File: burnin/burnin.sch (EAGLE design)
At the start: 12 parts, among them M1 ARDUINO_R3_ICSP_NODIM, U1 TXB0104PWR

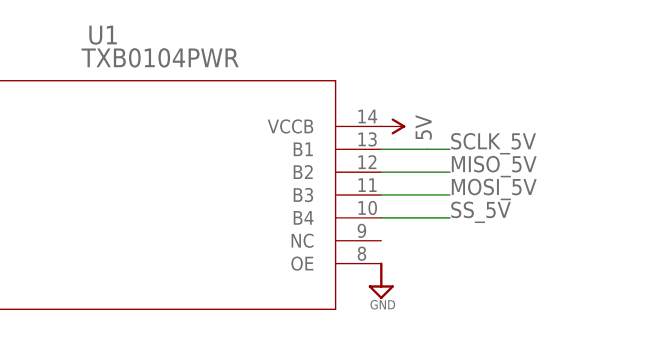
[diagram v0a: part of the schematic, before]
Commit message: fix burnin OE and make QFP MIPPE
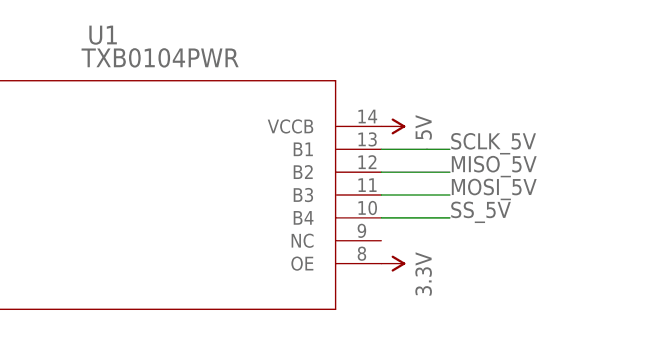
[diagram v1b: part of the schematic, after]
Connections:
- net 3.3V: now also U1.OE
- net GND: no longer U1.OE
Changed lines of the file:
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@@
 <?xml version="1.0" encoding="utf-8"?>
 <!DOCTYPE eagle SYSTEM "eagle.dtd">
-<eagle version="9.4.2">
+<eagle version="9.5.0">
 <drawing>
 <settings>
@@
 <part name="FRAME1" library="scono" deviceset="FRAME_SCHEMATIC" device="">
 <attribute name="AUTHOR" value="S. Ono"/>
-<attribute name="REV" value="A"/>
+<attribute name="REV" value="B"/>
 <attribute name="SUBSYSTEM_NAME" value="bootloader"/>
 </part>
@@
 <part name="J1" library="scono" deviceset="CONN_02" device="" package3d_urn="urn:adsk.eagle:package:38039/1"/>
 <part name="U1" library="scono" deviceset="TXB0104PWR" device=""/>
-<part name="SUPPLY1" library="scono" deviceset="GND" device=""/>
 <part name="SUPPLY2" library="scono" deviceset="GND" device=""/>
 <part name="SUPPLY3" library="scono" deviceset="GND" device=""/>
@@
 <part name="SUPPLY10" library="scono" deviceset="GND" device=""/>
 <part name="SUPPLY11" library="scono" deviceset="GND" device=""/>
+<part name="U$8" library="scono" deviceset="3.3V" device=""/>
 </parts>
 <sheets>
@@
 <attribute name="VALUE" x="172.4406" y="77.6986" size="2.0828" layer="96" ratio="6" rot="SR0"/>
 </instance>
-<instance part="SUPPLY1" gate="GND" x="205.74" y="53.34" smashed="yes">
-<attribute name="VALUE" x="204.47" y="50.8" size="1.016" layer="96"/>
-</instance>
 <instance part="SUPPLY2" gate="GND" x="149.86" y="53.34" smashed="yes">
 <attribute name="VALUE" x="148.59" y="50.8" size="1.016" layer="96"/>
@@
 <instance part="SUPPLY11" gate="GND" x="228.6" y="142.24" smashed="yes" rot="R180">
 <attribute name="VALUE" x="229.87" y="144.78" size="1.016" layer="96" rot="R180"/>
+</instance>
+<instance part="U$8" gate="G$1" x="205.74" y="55.88" smashed="yes" rot="R270">
+<attribute name="VALUE" x="209.55" y="57.15" size="1.778" layer="96" rot="R270"/>
 </instance>
 </instances>
@@
 <net name="GND" class="0">
 <segment>
-<pinref part="U1" gate="A" pin="OE"/>
-<pinref part="SUPPLY1" gate="GND" pin="GND"/>
-</segment>
-<segment>
 <pinref part="U1" gate="A" pin="GND"/>
 <pinref part="SUPPLY2" gate="GND" pin="GND"/>
@@
 <pinref part="U$6" gate="G$1" pin="3.3V"/>
 </segment>
+<segment>
+<pinref part="U1" gate="A" pin="OE"/>
+<pinref part="U$8" gate="G$1" pin="3.3V"/>
+</segment>
 </net>

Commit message: finish 32u4 and rev c burnin
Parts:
- added ISP2: AVRISP-6, scono:AVRISP-6
- added J2: (no value), scono:CONN_02
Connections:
- net 5V: now also ISP2.VCC
- net GND: now also ISP2.GND
- net MISO_5V: now also ISP2.MISO
- net MOSI_5V: now also ISP2.MOSI
- net SCLK_5V: now also ISP2.SCK
- net SS_5V: now also ISP2.RST
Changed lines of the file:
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@@
 <?xml version="1.0" encoding="utf-8"?>
 <!DOCTYPE eagle SYSTEM "eagle.dtd">
-<eagle version="9.5.0">
+<eagle version="9.5.1">
 <drawing>
 <settings>
-<setting alwaysvectorfont="no"/>
+<setting alwaysvectorfont="yes"/>
 <setting verticaltext="up"/>
 </settings>
@@
 <part name="FRAME1" library="scono" deviceset="FRAME_SCHEMATIC" device="">
 <attribute name="AUTHOR" value="S. Ono"/>
-<attribute name="REV" value="B"/>
+<attribute name="REV" value="C"/>
 <attribute name="SUBSYSTEM_NAME" value="bootloader"/>
 </part>
@@
 <part name="SUPPLY11" library="scono" deviceset="GND" device=""/>
 <part name="U$8" library="scono" deviceset="3.3V" device=""/>
+<part name="ISP2" library="scono" deviceset="AVRISP" device="-6"/>
+<part name="J2" library="scono" deviceset="CONN_02" device="" package3d_urn="urn:adsk.eagle:package:38039/1"/>
+<part name="U$9" library="scono" deviceset="5V" device=""/>
+<part name="SUPPLY1" library="scono" deviceset="GND" device=""/>
 </parts>
 <sheets>
@@
 <attribute name="VALUE" x="209.55" y="57.15" size="1.778" layer="96" rot="R270"/>
 </instance>
+<instance part="ISP2" gate="G$1" x="55.88" y="33.02" smashed="yes">
+<attribute name="NAME" x="53.34" y="25.4" size="1.778" layer="95"/>
+</instance>
+<instance part="J2" gate="G$1" x="66.04" y="12.7" smashed="yes">
+<attribute name="VALUE" x="63.5" y="7.874" size="1.778" layer="96" font="vector"/>
+<attribute name="NAME" x="63.5" y="18.288" size="1.778" layer="95" font="vector"/>
+</instance>
+<instance part="U$9" gate="G$1" x="73.66" y="35.56" smashed="yes" rot="R270">
+<attribute name="VALUE" x="77.47" y="36.83" size="1.778" layer="96" rot="R270"/>
+</instance>
+<instance part="SUPPLY1" gate="GND" x="71.12" y="27.94" smashed="yes">
+<attribute name="VALUE" x="69.85" y="25.4" size="1.016" layer="96"/>
+</instance>
 </instances>
 <busses>
@@
 <pinref part="SUPPLY11" gate="GND" pin="GND"/>
 </segment>
+<segment>
+<pinref part="ISP2" gate="G$1" pin="GND"/>
+<pinref part="SUPPLY1" gate="GND" pin="GND"/>
+</segment>
 </net>
 <net name="3.3V" class="0">
@@
 <pinref part="C2" gate="G$1" pin="2"/>
 <pinref part="U$7" gate="G$1" pin="5V"/>
+</segment>
+<segment>
+<pinref part="ISP2" gate="G$1" pin="VCC"/>
+<pinref part="U$9" gate="G$1" pin="5V"/>
+<wire x1="71.12" y1="35.56" x2="73.66" y2="35.56" width="0.1524" layer="91"/>
 </segment>
 </net>
@@
 <label x="213.36" y="68.58" size="1.778" layer="95"/>
 </segment>
+<segment>
+<pinref part="ISP2" gate="G$1" pin="SCK"/>
+<wire x1="43.18" y1="33.02" x2="38.1" y2="33.02" width="0.1524" layer="91"/>
+<label x="27.94" y="33.02" size="1.778" layer="95"/>
+</segment>
 </net>
 <net name="MISO_5V" class="0">
@@
 <label x="213.36" y="66.04" size="1.778" layer="95"/>
 </segment>
+<segment>
+<pinref part="ISP2" gate="G$1" pin="MISO"/>
+<wire x1="43.18" y1="35.56" x2="38.1" y2="35.56" width="0.1524" layer="91"/>
+<label x="27.94" y="35.56" size="1.778" layer="95"/>
+</segment>
 </net>
 <net name="MOSI_5V" class="0">
@@
 <wire x1="205.74" y1="63.5" x2="213.36" y2="63.5" width="0.1524" layer="91"/>
 <label x="213.36" y="63.5" size="1.778" layer="95"/>
+</segment>
+<segment>
+<pinref part="ISP2" gate="G$1" pin="MOSI"/>
+<wire x1="71.12" y1="33.02" x2="76.2" y2="33.02" width="0.1524" layer="91"/>
+<label x="83.82" y="33.02" size="1.778" layer="95"/>
 </segment>
 </net>
@@
 <label x="213.36" y="60.96" size="1.778" layer="95"/>
 </segment>
-</net>
+<segment>
+<pinref part="ISP2" gate="G$1" pin="RST"/>
+<wire x1="43.18" y1="30.48" x2="38.1" y2="30.48" width="0.1524" layer="91"/>
+<label x="27.94" y="30.48" size="1.778" layer="95"/>
+</segment>
+</net>

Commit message: blaaahhhhh 328pb worked
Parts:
- removed C1, C2: 0.1uF, scono:CAP0603-CAP
- removed ISP2: AVRISP-6, scono:AVRISP-6
- removed J2: (no value), scono:CONN_02
- removed U1: TXB0104PWR, scono:TXB0104PWR
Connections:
- removed net MISO_3V: ISP1.MISO, U1.A2
- removed net MOSI_3V: ISP1.MOSI, U1.A3
- removed net SCLK_3V: ISP1.SCK, U1.A1
- removed net SS_3V: ISP1.RST, U1.A4
- net 3.3V: no longer C1.2, ISP1.VCC, U1.OE, U1.VCCA
- net 5V: now also ISP1.VCC; no longer C2.2, ISP2.VCC, U1.VCCB
- net GND: no longer C1.1, C2.1, ISP2.GND, U1.GND
- net MISO_5V: now also ISP1.MISO; no longer ISP2.MISO, U1.B2
- net MOSI_5V: now also ISP1.MOSI; no longer ISP2.MOSI, U1.B3
- net SCLK_5V: now also ISP1.SCK; no longer ISP2.SCK, U1.B1
- net SS_5V: now also ISP1.RST; no longer ISP2.RST, U1.B4
